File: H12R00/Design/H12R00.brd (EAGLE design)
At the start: 34.6 x 30 mm, 32 parts, among them P1 HEXABIT_17.32_NO_P3_P6, U1 STM32F091CBU6, U2 AD628ARZ, X1 XTALL_CSTCE8M00G52

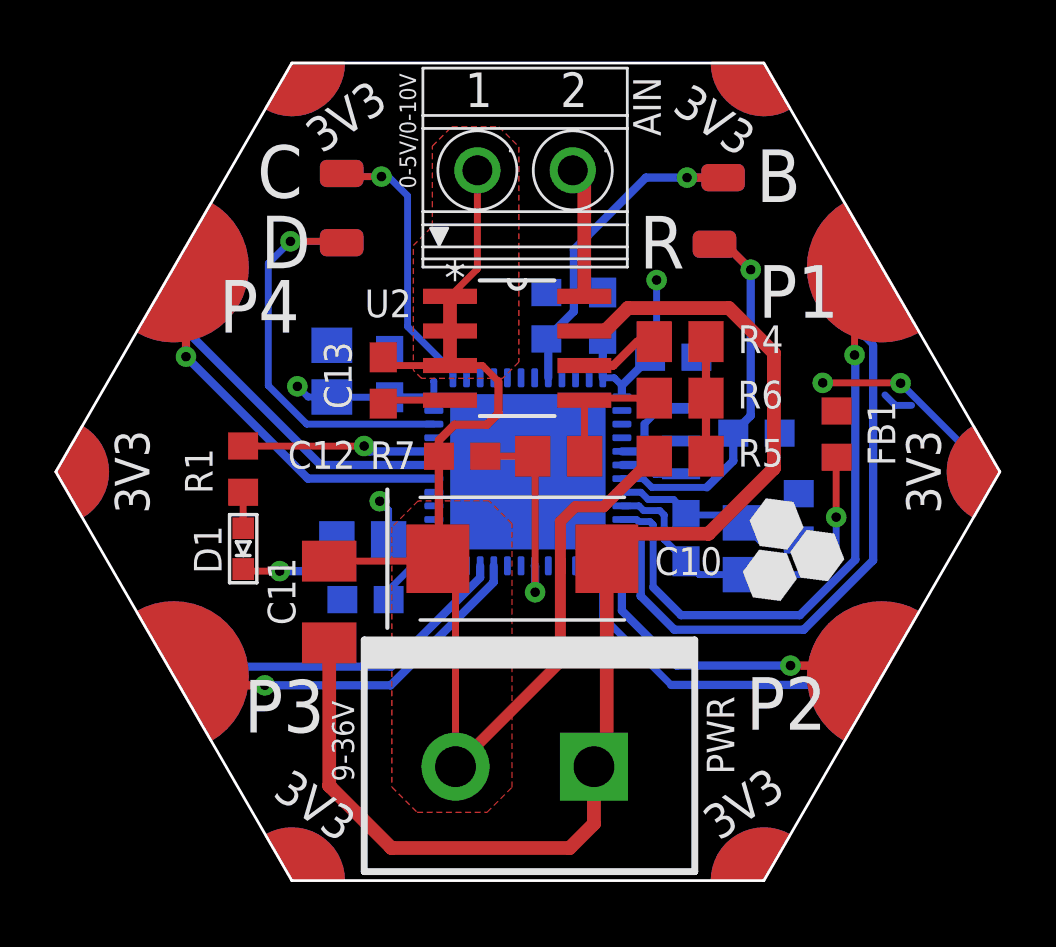
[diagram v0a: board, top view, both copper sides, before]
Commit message: changed schematic design and modifies PCB (output files were not updated)
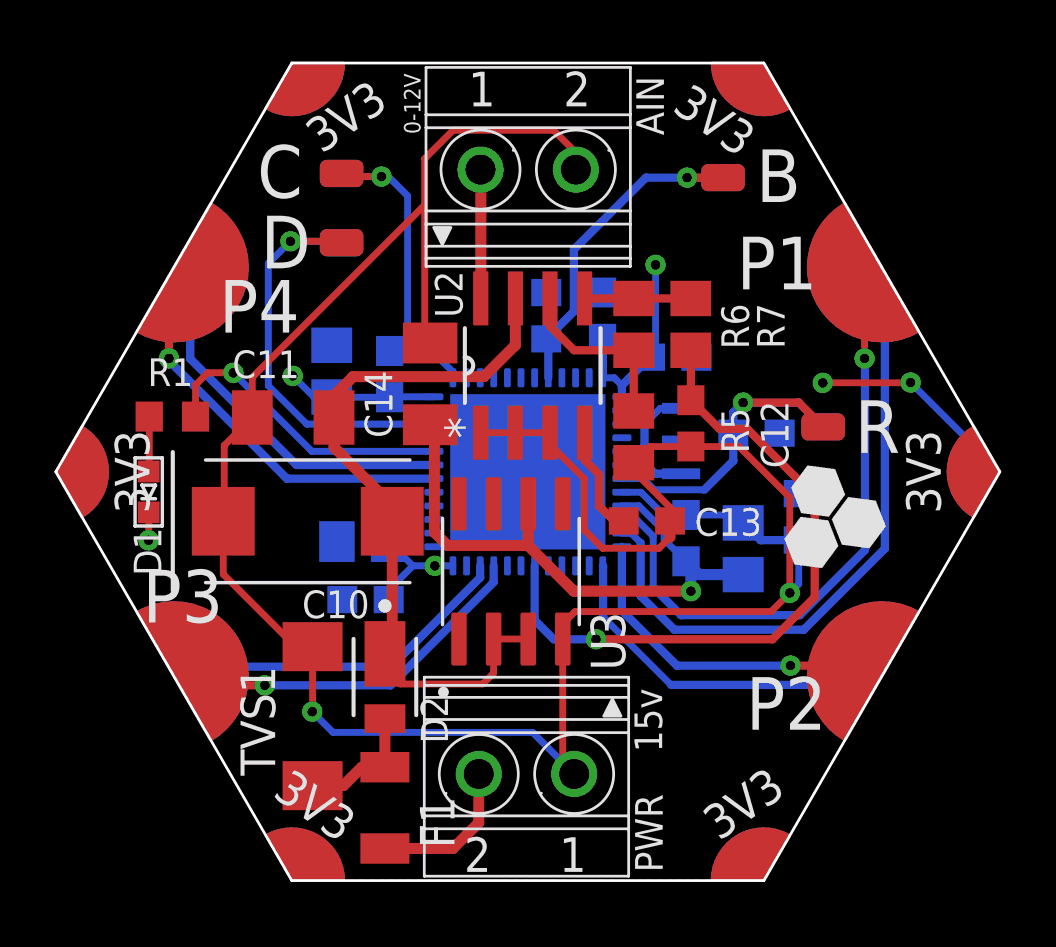
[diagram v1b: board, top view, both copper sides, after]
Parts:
- removed FB1: FB-TDK_MMZ1608Y300B, Hexabitz:FB-TDK_MMZ1608Y300B
- removed R4: 3.9 kΩ, Hexabitz:R-0805
- added C14: 100 nF, Hexabitz:C1206K
- added D2: DIODES_SBR2U30P1-7DIODES_SBR2U30P1-7_0_0, Hexabitz:DIODES_SBR2U30P1-7_0
- added F1: NANOSMDC035F-2120, Hexabitz:R1206
- added TVS1: SMBJ30CA, Hexabitz:DO214AA
- added U3: REF193GSZ, Hexabitz:SOIC127P600X172-8N
- PWR: value (none) -> CON-PHOENIX-350_1751248; device Hexabitz:1546111-2 -> Hexabitz:CON-PHOENIX-350_1751248
- moved C13 11.0 mm to (39.0, 32.8), turned to 0 degrees
- moved C12 8.48 mm to (40.6, 36.4), turned to 270 degrees
- moved C10 7.99 mm to (26.5, 32.8)
- moved R 7.80 mm to (45.5, 36.3)
- moved C11 6.90 mm to (26.0, 36.6), turned to 180 degrees
- moved R7 6.85 mm to (40.6, 40.0), turned to 90 degrees
- moved D1 4.04 mm to (20.7, 33.9)
- moved R1 3.23 mm to (21.6, 36.6), turned to 0 degrees
- moved R6 3.20 mm to (38.5, 40.0), turned to 270 degrees
- moved R5 1.84 mm to (38.5, 35.9), turned to 90 degrees
- moved U2 0.85 mm to (34.8, 38.5), turned to 90 degrees
- moved PWR 0.37 mm to (34.6, 23.4)
- moved AIN 0.12 mm to (34.6, 45.8)
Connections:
- removed net AGND: AIN.1, C10.2, C11.2, C12.2, C13.2, PWR.2, R5.2, U2.1, U2.2, U2.3
- removed net VDDA: C1.1, C2.1, FB1.1, U1.P$9
- removed net VS: C10.1, C11.1, PWR.1, U2.7
- new net +15V: C10.1, C11.1, D2.1, U2.7, U3.2, U3.3
- new net 3V0: C1.1, C14.1, C2.1, U1.P$9, U3.6
- new net N$10: D2.2, F1.2, TVS1.C
- net N$2: now also R5.2, R6.2; no longer R4.1
- net N$8: now also F1.1, PWR.2; no longer R4.2, R5.1, R6.2
- net VDD: no longer FB1.2
- net VIN: now also AIN.1; no longer AIN.2
- net VSSA: now also AIN.2, C10.2, C11.2, C12.2, C13.2, C14.2, PWR.1, R5.1, TVS1.A, U2.1, U2.2, U2.3, U3.4
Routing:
- net VSSA: track 7.29 -> 95.3 mm, vias 0 -> 2
- net AGND: track 47.2 -> 0.00 mm
- net VS: track 45.9 -> 0.00 mm
- net +15V: track 0.00 -> 27.1 mm
- net 3V0: track 0.00 -> 22.7 mm, vias 0 -> 1
- net AI: track 7.75 -> 24.7 mm
- net VDDA: track 13.5 -> 0.00 mm, vias 1 -> 0
- net N$10: track 0.00 -> 4.72 mm
- net N$3: track 7.08 -> 11.3 mm
- net GND: track 12.3 -> 8.56 mm
- net N$2: track 2.93 -> 6.68 mm
- net N$11: track 2.50 -> 4.04 mm
- net N$8: track 4.20 -> 5.62 mm
- net VDD: track 19.2 -> 17.9 mm
- net R1: track 15.3 -> 14.2 mm
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- removed copper zone on layer 1, net AGND
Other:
- board text added: "0-12V"
- board text added: "15v"
- board text removed: "0-5V/0-10V"
- board text removed: "9-36V"

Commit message: PCB modifications and output files were generated
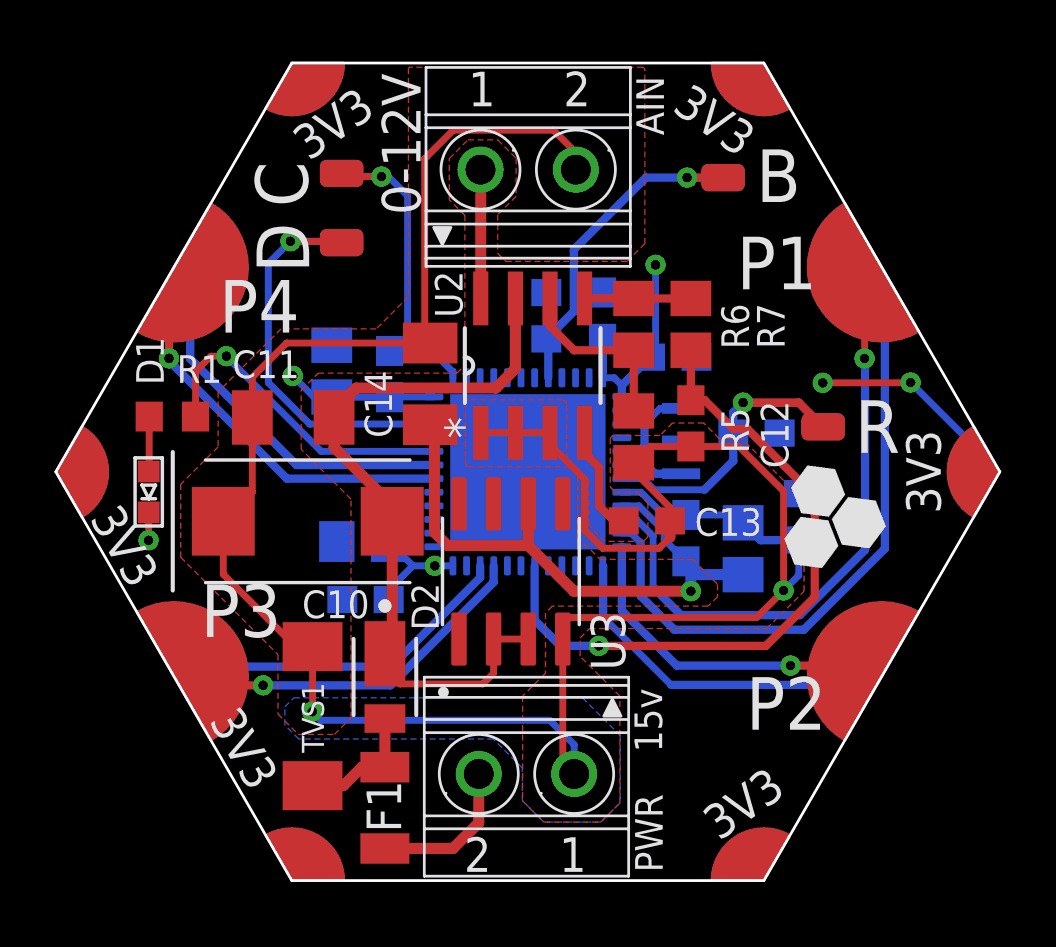
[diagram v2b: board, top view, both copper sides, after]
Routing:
- net VSSA: track 95.3 -> 93.7 mm
- net N$3: track 11.3 -> 12.1 mm
- net R1: track 14.2 -> 13.6 mm
- added copper zone on layer 1, net VSSA
- added copper zone on layer 16, net VSSA
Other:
- board text added: "0-12v"

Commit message: Update some components from lib. REF is missing in lib
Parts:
- C13: value 15 nF -> 15nF
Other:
- board text added: "P2*"
- board text added: "P4*"
- board text removed: "P2"
- board text removed: "P4"
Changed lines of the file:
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@@
 <text x="49.14" y="34.62" size="1.27" layer="22" font="vector" rot="MR90" align="center">GND</text>
 <text x="42.5277" y="22.4564" size="1.27" layer="21" font="vector" rot="R35" align="center">3V3</text>
-<text x="42.5277" y="22.4691" size="1.27" layer="22" font="vector" rot="MR325" align="center">GND</text>
+<text x="41.6387" y="22.1135" size="1.27" layer="22" font="vector" rot="MR325" align="center">GND</text>
 <text x="24.2161" y="24.4771" size="1.27" layer="21" font="vector" rot="R120" align="center">3V3</text>
-<text x="26.8266" y="22.3548" size="1.27" layer="22" font="vector" rot="MR35" align="center">GND</text>
+<text x="27.2457" y="22.1516" size="1.27" layer="22" font="vector" rot="MR35" align="center">GND</text>
 <text x="19.8333" y="31.9022" size="1.27" layer="21" font="vector" rot="R120" align="center">3V3</text>
 <text x="20.1" y="34.62" size="1.27" layer="22" font="vector" rot="MR90" align="center">GND</text>
@@
 <text x="27.9188" y="47.6726" size="1.27" layer="22" font="vector" rot="MR325" align="center">GND</text>
 <text x="43.7615" y="42.2812" size="1.9304" layer="21" font="vector" align="center">P1</text>
-<text x="43.7742" y="42.2812" size="1.9304" layer="22" font="vector" rot="MR0" align="center">P1</text>
-<text x="44.1044" y="26.1206" size="1.9304" layer="21" font="vector" align="center">P2</text>
-<text x="44.079" y="26.0952" size="1.9304" layer="22" font="vector" rot="MR0" align="center">P2</text>
+<text x="43.698" y="41.2017" size="1.9304" layer="22" font="vector" rot="MR0" align="center">P1</text>
+<text x="43.1646" y="27.289" size="1.9304" layer="21" font="vector" align="center">P2*</text>
+<text x="42.9868" y="26.6921" size="1.9304" layer="22" font="vector" rot="MR0" align="center">P2*</text>
 <text x="24.0942" y="29.5242" size="1.9304" layer="21" font="vector" align="center">P3</text>
-<text x="21.9352" y="30.083" size="1.9304" layer="22" font="vector" rot="MR0" align="center">P3</text>
-<text x="24.7673" y="40.6937" size="1.9304" layer="21" font="vector" align="center">P4</text>
-<text x="24.78" y="40.6937" size="1.9304" layer="22" font="vector" rot="MR0" align="center">P4</text>
+<text x="25.6817" y="26.9207" size="1.9304" layer="22" font="vector" rot="MR0" align="center">P3</text>
+<text x="25.7833" y="40.6175" size="1.9304" layer="21" font="vector" align="center">P4*</text>
+<text x="23.6116" y="39.4872" size="1.9304" layer="22" font="vector" rot="MR0" align="center">P4*</text>
 <text x="35.052" y="27.636725" size="1.9304" layer="22" font="vector" rot="MR0" align="center">H12R00</text>
 <rectangle x1="45.40376875" y1="31.080203125" x2="45.4185" y2="31.094934375" layer="21"/>
@@
 <attribute name="VALUE" x="32.5804" y="49.9364" size="1.27" layer="27"/>
 </element>
-<element name="C13" library="Hexabitz" package="C-0603" value="15 nF" x="38.989" y="32.8168" smashed="yes">
+<element name="C13" library="Hexabitz" package="C-0603" value="15nF" x="38.989" y="32.8168" smashed="yes">
 <attribute name="CAPACITANCE" value="" x="38.989" y="32.8168" size="1.778" layer="27" display="off"/>
 <attribute name="MFN" value="" x="38.989" y="32.8168" size="1.778" layer="27" display="off"/>
@@
 <contactref element="P1" pad="PAD_PD11"/>
 <contactref element="P1" pad="PAD_PD12"/>
-<polygon width="0.1016" layer="16" isolate="0.1016" thermals="no">
+<polygon width="0.1016" layer="16" isolate="0.1016" thermals="no" rank="2">
 <vertex x="25.960325" y="19.6207375"/>
 <vertex x="43.280075" y="19.6207375"/>
@@
 <contactref element="P1" pad="PAD_PU11"/>
 <contactref element="P1" pad="PAD_PU12"/>
-<polygon width="0.1016" layer="1" isolate="0.1016" thermals="no">
+<polygon width="0.1016" layer="1" isolate="0.1016" thermals="no" rank="2">
 <vertex x="25.960325" y="19.6207375"/>
 <vertex x="43.280075" y="19.6207375"/>
@@
 <via x="39.3065" y="42.2148" extent="1-16" drill="0.35"/>
 <via x="31.2039" y="31.17019375" extent="1-16" drill="0.35"/>
+<wire x1="29.511284375" y1="32.060890625" x2="29.5475625" y2="37.355915625" width="0" layer="19" extent="16-16"/>
+<wire x1="37.3702" y1="38.07020625" x2="31.17019375" y2="37.3702" width="0" layer="19" extent="16-16"/>
+<wire x1="18.1002" y1="34.6202" x2="25.9969" y2="38.1381" width="0" layer="19" extent="1-1"/>
 </signal>
 <signal name="UART3_TX">
@@
 <contactref element="U2" pad="8"/>
 <contactref element="AIN" pad="1"/>
-<wire x1="32.893" y1="40.9829" x2="32.893" y2="45.6988" width="0.4064" layer="1"/>
+<wire x1="32.893" y1="40.9829" x2="32.893" y2="45.6988" width="0.6096" layer="1"/>
 <wire x1="32.893" y1="45.6988" x2="32.8829" y2="45.7089" width="0.254" layer="1"/>
 </signal>

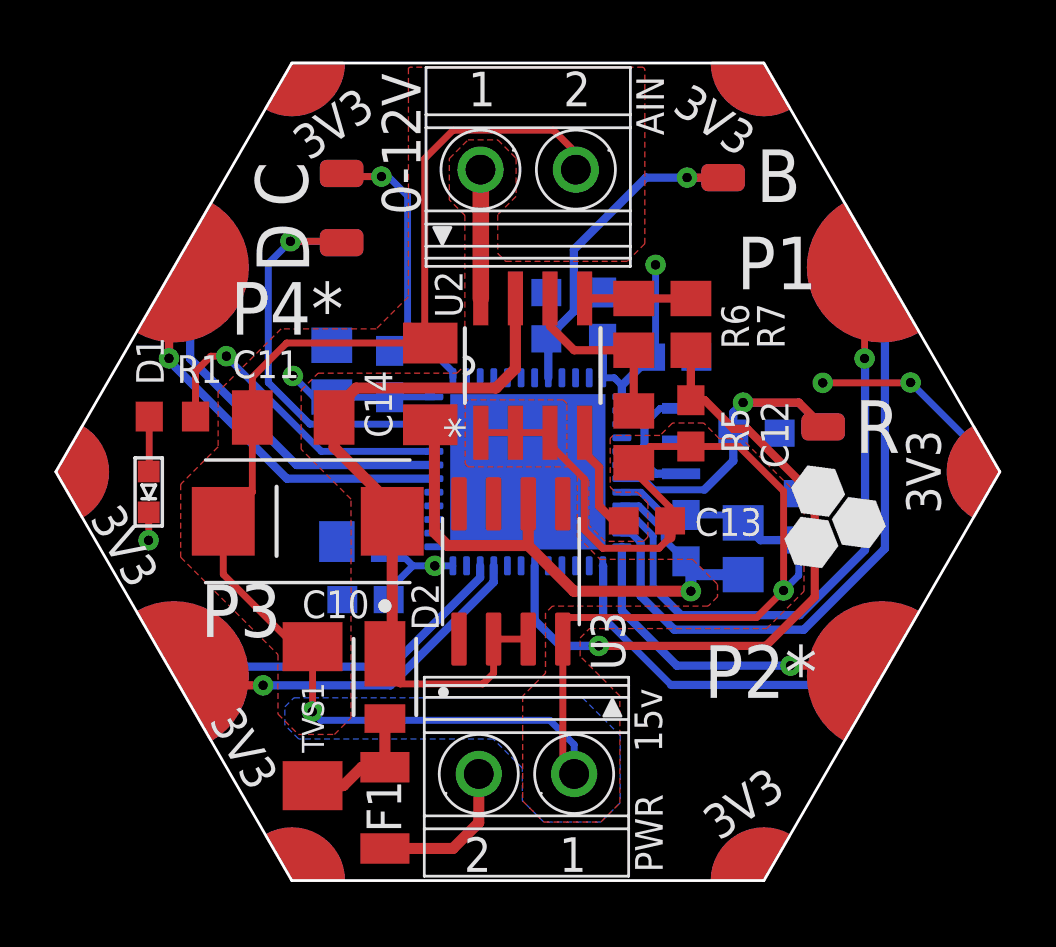
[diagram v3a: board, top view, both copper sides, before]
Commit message: Update REF from library Fix routing and DRC issues
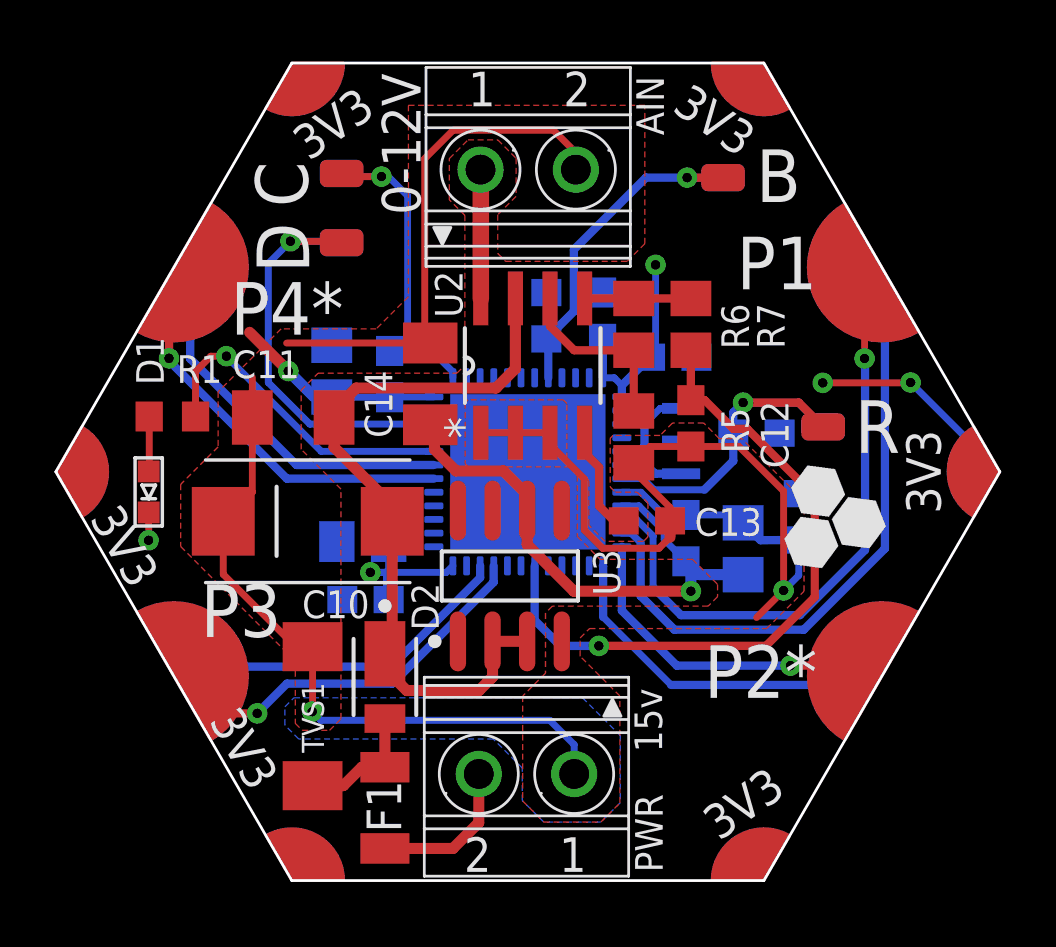
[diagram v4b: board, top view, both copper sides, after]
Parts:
- U3: device Hexabitz:SOIC127P600X172-8N -> Hexabitz:REF193GSZ_1
- moved U3 0.17 mm to (34.0, 30.8)
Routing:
- net VSSA: track 93.7 -> 79.0 mm
- net VDD: track 17.9 -> 21.8 mm
- net 3V0: track 22.7 -> 20.5 mm
- net UART3_TX: track 13.6 -> 14.4 mm
